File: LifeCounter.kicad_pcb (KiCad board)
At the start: 4 copper layers, 132.3 x 43.9 mm, 36 parts, among them IC1 STM32H562RGT6, IC2 AP3012KTR-E1, IC3 MCP73831T-2ATI_OT, IC4 AP2112K-3.3TRG1, J1 54104-4531, J2 USB_C_Receptacle_USB2.0_14P

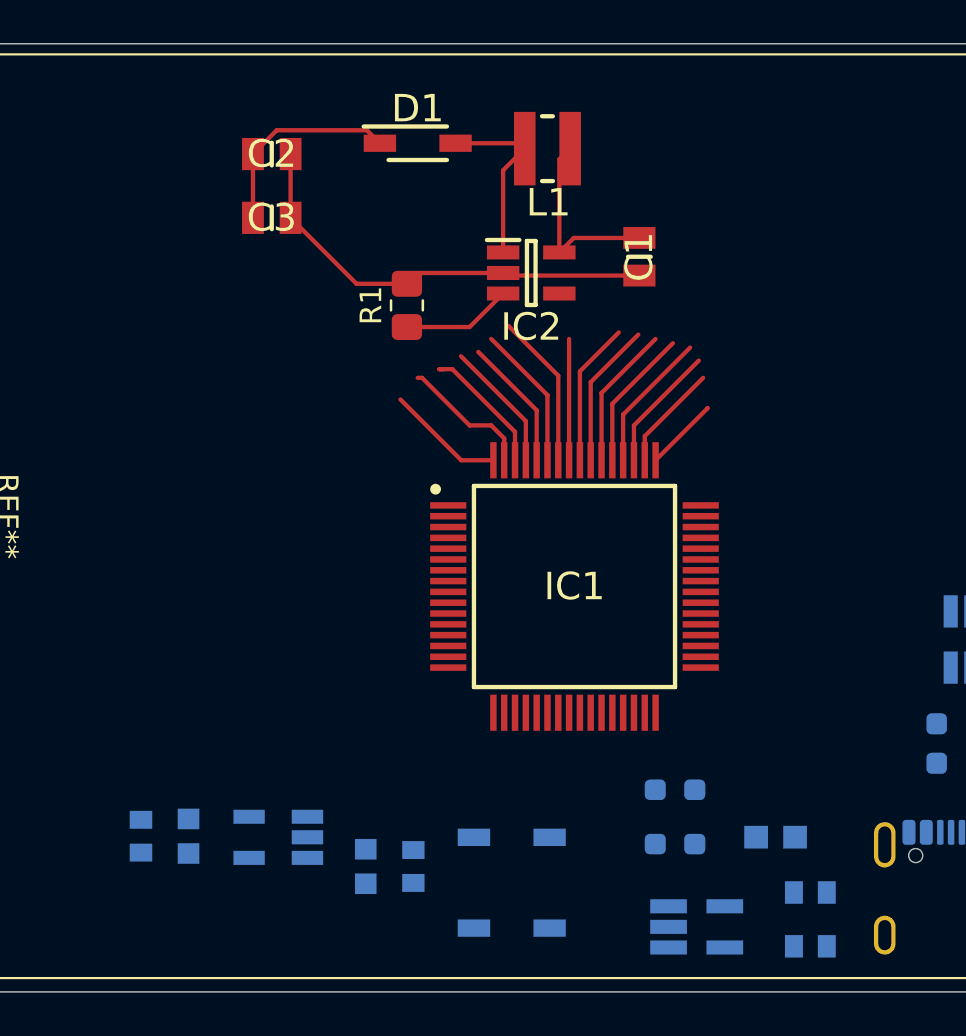
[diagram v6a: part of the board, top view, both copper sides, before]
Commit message: capacitor changes
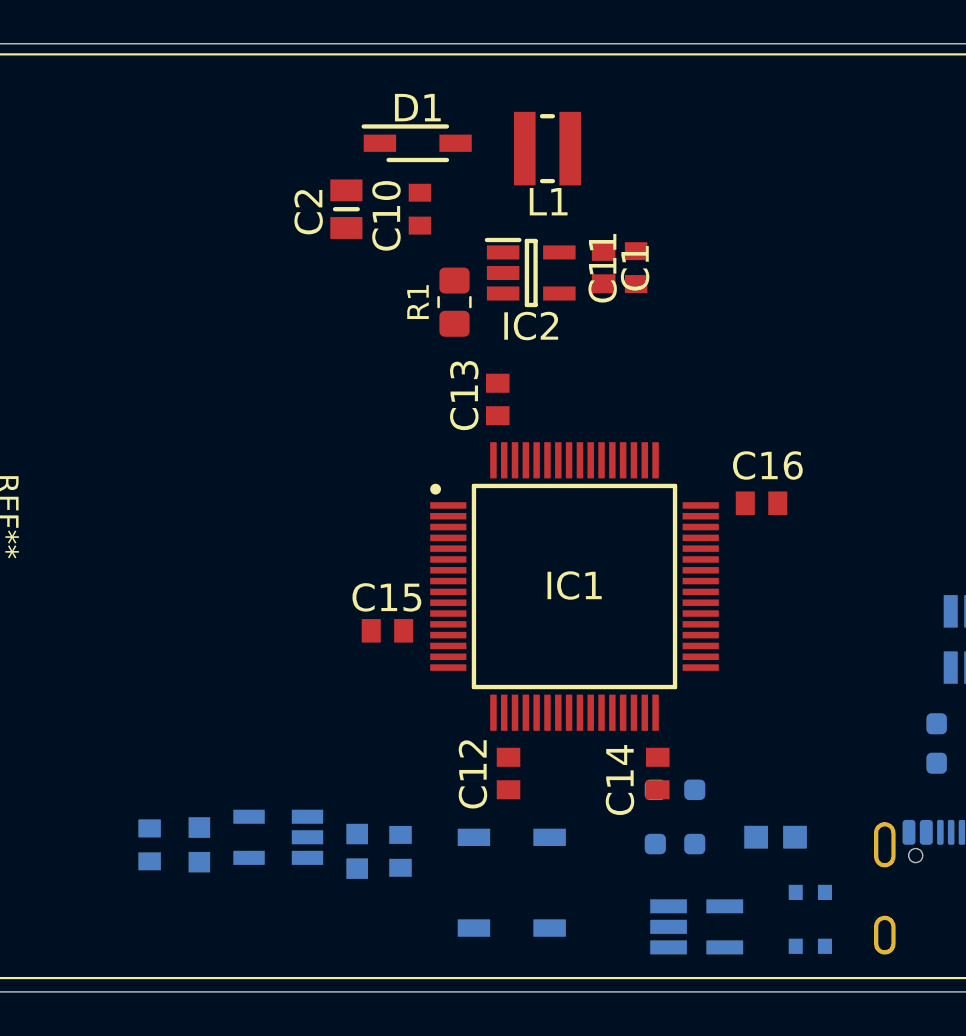
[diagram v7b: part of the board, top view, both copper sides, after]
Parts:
- added C11: 06033D104KAT2A, LifeCounter-Footprints:Kyocera_CAPC1608X90M, F.Cu at (173.6, 71.5)
- added C12: 06033D104KAT2A, LifeCounter-Footprints:Kyocera_CAPC1608X90M, F.Cu at (169.2, 94.9)
- added C13: 06033D104KAT2A, LifeCounter-Footprints:Kyocera_CAPC1608X90M, F.Cu at (168.7, 77.6)
- added C14: 06033D104KAT2A, LifeCounter-Footprints:Kyocera_CAPC1608X90M, F.Cu at (176.1, 94.9)
- added C15: 06033D104KAT2A, LifeCounter-Footprints:Kyocera_CAPC1608X90M, F.Cu at (163.6, 88.3)
- added C16: 06033D104KAT2A, LifeCounter-Footprints:Kyocera_CAPC1608X90M, F.Cu at (180.9, 82.4)
- C1: value CL21B105KBFNNNE -> CL10B105KO8NNNC; footprint LifeCounter-Footprints:Samsung_CAPC2012X135M -> LifeCounter-Footprints:Samsung_CAPC1608X90M
- C10: value C0603C104K8RACTU -> CL10B104KB8NNNC; footprint LifeCounter-Footprints:Kemet_C0603 -> LifeCounter-Footprints:Samsung_CAPC1608X90M; moved to F.Cu
- C3: value CL21B105KBFNNNE -> CL10B105KO8NNNC; footprint LifeCounter-Footprints:Samsung_CAPC2012X135M -> LifeCounter-Footprints:Samsung_CAPC1608X90M; moved to B.Cu
- C5, C6: value CL10A475KP8NNNC -> GRM188R61E106KA73D; footprint LifeCounter-Footprints:Samsung_CAPC1608X90M -> LifeCounter-Footprints:Murata_GRM18x
- C7: value CL10A106KP8NNNC -> CL10B105KO8NNNC
- C9: value CL10A106KP8NNNC -> C0603C104K8RACTU; footprint LifeCounter-Footprints:Samsung_CAPC1608X90M -> LifeCounter-Footprints:Kemet_C0603
- moved C10 30.9 mm to (165.1, 68.8)
- moved C3 29.5 mm to (152.6, 98.2), turned to -90 degrees
- moved C2 4.29 mm to (161.7, 68.8), turned to -90 degrees
- moved C9 2.73 mm to (154.9, 98.2)
- moved R1 2.21 mm to (166.7, 73.1)
- moved C7 0.92 mm to (164.2, 98.5)
- moved C8 0.81 mm to (162.2, 98.5)
- moved C1 0.52 mm to (175.1, 71.5)
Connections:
- C1 pad 2: Net-(IC2-GND) -> GND
- C10 pad 1: +3V3 -> Net-(D1-K)
- C2 pad 2: Net-(IC2-GND) -> GND
- C3 pad 1: Net-(D1-K) -> +3V3
- C3 pad 2: Net-(IC2-GND) -> GND
- C5 pad 1: /VBUS -> Net-(BT1-+)
- C6 pad 1: Net-(BT1-+) -> /VBUS
- IC2 pad 2: Net-(IC2-GND) -> GND
- R1 pad 2: Net-(IC2-GND) -> GND
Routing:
- net Net-(IC2-GND): track 20.6 -> 0.00 mm
- net Net-(D1-K): track 9.52 -> 0.00 mm
- net Net-(IC2-VIN): track 8.98 -> 0.00 mm
- net Net-(D1-A): track 8.52 -> 0.00 mm
- net unconnected-(IC1-PB6-Pad58): track 7.16 -> 0.00 mm
- net unconnected-(IC1-PB3-Pad55): track 6.72 -> 0.00 mm
- net unconnected-(IC1-PB7-Pad59): track 6.69 -> 0.00 mm
- net unconnected-(IC1-PB4-Pad56): track 6.66 -> 0.00 mm
- net unconnected-(IC1-PD2-Pad54): track 6.65 -> 0.00 mm
- net unconnected-(IC1-PC12-Pad53): track 6.57 -> 0.00 mm
- net unconnected-(IC1-PC11-Pad52): track 6.50 -> 0.00 mm
- net GND: track 6.45 -> 0.00 mm
- net unconnected-(IC1-VCAP_2-Pad62): track 6.21 -> 0.00 mm
- net unconnected-(IC1-BOOT0-Pad60): track 6.13 -> 0.00 mm
- net unconnected-(IC1-PB8-Pad61): track 6.05 -> 0.00 mm
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
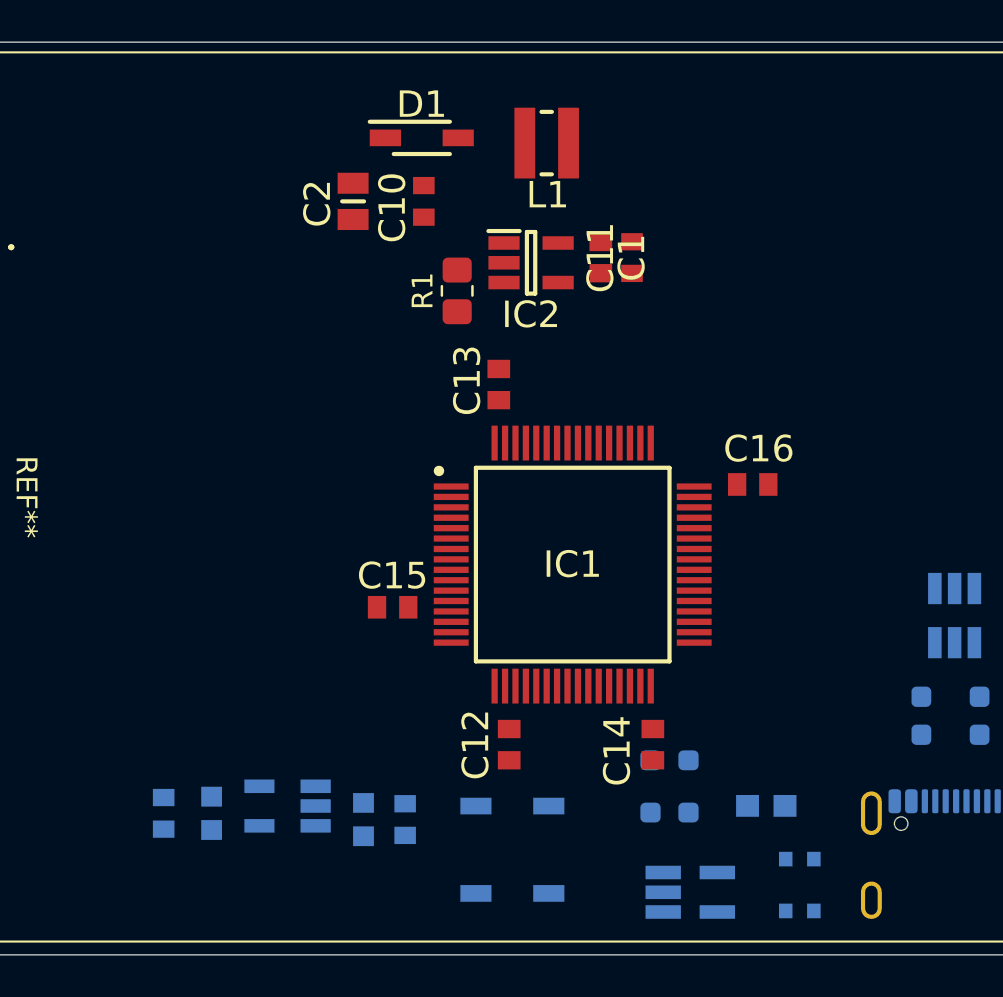
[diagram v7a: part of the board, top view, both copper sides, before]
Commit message: labeled the LCD pins and switched over to a 100 pin stm32 package
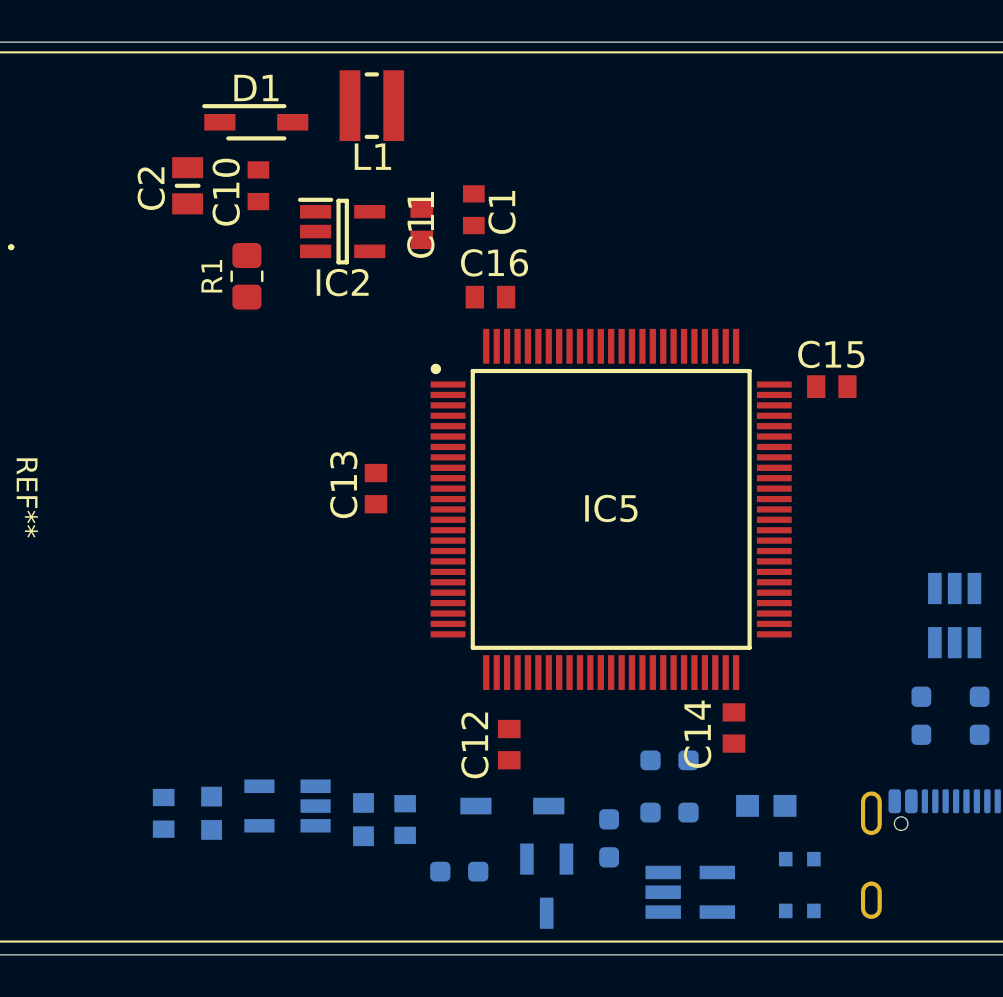
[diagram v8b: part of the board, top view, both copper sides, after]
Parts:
- removed D3: 1N5819HWQ-7-F, LifeCounter-Footprints:Diodes-Inc_SOD3716X145M
- removed IC1: STM32H562RGT6, LifeCounter-Footprints:LQFP-64_10x10mm_P0.5mm_STM32
- added IC5: STM32H562VGT6, LifeCounter-Footprints:STMicroelectronics_QFP50P1600X1600X160-100M, F.Cu at (174.1, 83.6)
- added Q1: AO3401A, LifeCounter-Footprints:Alpha&Omega_SOT95P280X125-3M, B.Cu at (171.0, 101.7)
- added R6: 100k, Resistor_SMD:R_0603_1608Metric_Pad0.98x0.95mm_HandSolder, B.Cu at (166.8, 101.0)
- added R7: 1k, Resistor_SMD:R_0603_1608Metric_Pad0.98x0.95mm_HandSolder, B.Cu at (174.0, 99.4)
- C1, C3, C7: value CL10B105KO8NNNC -> 1uF
- C10: value CL10B104KB8NNNC -> 100nF
- C11, C12, C13, C14, C15, C16: value 06033D104KAT2A -> 100nF
- C2: value CL21B105KBFNNNE -> 1uF
- C4: value CL10A106KP8NNNC -> 10uF
- C5, C6: value GRM188R61E106KA73D -> 10uF
- C8, C9: value C0603C104K8RACTU -> 100nF
- L1: value VLS3012CX-100M-1 -> 10uH
- R1: value 0805S8F820JT5E -> 62
- R4: value 2k -> 2k7
- moved C15 23.6 mm to (184.7, 77.7)
- moved C16 15.5 mm to (168.3, 73.4)
- moved R1 10.1 mm to (156.6, 72.4)
- moved IC2 9.17 mm to (161.2, 70.2)
- moved C11 8.75 mm to (165.0, 69.9)
- moved L1 8.59 mm to (162.6, 64.2)
- moved C10 7.99 mm to (157.2, 68.0)
- moved C2 7.99 mm to (153.8, 68.0)
- moved D1 7.99 mm to (157.1, 65.0)
- moved C1 7.94 mm to (167.5, 69.2)
- moved C13 7.73 mm to (162.8, 82.6)
- moved C14 3.98 mm to (180.0, 94.1)
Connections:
- net /VBUS renamed /Power_Management/VBUS
- net Net-(BT1-+) renamed /Power_Management/BAT+
- C10 pad 1: Net-(D1-K) -> /LCD_ANODE
- C12 pad 1: GND -> +3V3
- C12 pad 2: +3V3 -> GND
- C2 pad 1: Net-(D1-K) -> /LCD_ANODE
- D1 pad 1: Net-(D1-K) -> /LCD_ANODE
- IC2 pad 3: Net-(IC2-FB) -> /LCD_CATHODE
- IC2 pad 4: unconnected-(IC2-~{SHDN}-Pad4) -> /LCD_BL_EN
- J1 pad 10: unconnected-(J1-Pad10) -> GND
- J1 pad 11: unconnected-(J1-Pad11) -> GND
- J1 pad 12: unconnected-(J1-Pad12) -> GND
- J1 pad 13: unconnected-(J1-Pad13) -> GND
- J1 pad 14: unconnected-(J1-Pad14) -> GND
- J1 pad 15: unconnected-(J1-Pad15) -> GND
- J1 pad 16: unconnected-(J1-Pad16) -> GND
- J1 pad 17: unconnected-(J1-Pad17) -> GND
- J1 pad 18: unconnected-(J1-Pad18) -> GND
- J1 pad 19: unconnected-(J1-Pad19) -> GND
- J1 pad 2: unconnected-(J1-Pad2) -> GND
- J1 pad 20: unconnected-(J1-Pad20) -> GND
- J1 pad 21: unconnected-(J1-Pad21) -> /LCD_DB7
- J1 pad 22: unconnected-(J1-Pad22) -> /LCD_DB6
- J1 pad 23: unconnected-(J1-Pad23) -> /LCD_DB5
- J1 pad 24: unconnected-(J1-Pad24) -> /LCD_DB4
- J1 pad 25: unconnected-(J1-Pad25) -> /LCD_DB3
- J1 pad 26: unconnected-(J1-Pad26) -> /LCD_DB2
- J1 pad 27: unconnected-(J1-Pad27) -> /LCD_DB1
- J1 pad 28: unconnected-(J1-Pad28) -> /LCD_DB0
- J1 pad 29: unconnected-(J1-Pad29) -> /LCD_SDO
- J1 pad 3: unconnected-(J1-Pad3) -> GND
- J1 pad 30: unconnected-(J1-Pad30) -> +3V3
- J1 pad 31: unconnected-(J1-Pad31) -> /LCD_RD
- J1 pad 32: unconnected-(J1-Pad32) -> /LCD_RS
- J1 pad 33: unconnected-(J1-Pad33) -> /LCD_WR
- J1 pad 34: unconnected-(J1-Pad34) -> /LCD_CS
- J1 pad 35: unconnected-(J1-Pad35) -> /LCD_FMARK
- J1 pad 36: unconnected-(J1-Pad36) -> +3V3
- J1 pad 37: unconnected-(J1-Pad37) -> +3V3
- J1 pad 38: unconnected-(J1-Pad38) -> GND
- J1 pad 39: unconnected-(J1-Pad39) -> GND
- J1 pad 4: unconnected-(J1-Pad4) -> GND
- J1 pad 40: unconnected-(J1-Pad40) -> /LCD_ANODE
- J1 pad 41: unconnected-(J1-Pad41) -> /LCD_CATHODE
- J1 pad 5: unconnected-(J1-Pad5) -> GND
- J1 pad 6: unconnected-(J1-Pad6) -> /LCD_RESET
- J1 pad 7: unconnected-(J1-Pad7) -> +3V3
- J1 pad 8: unconnected-(J1-Pad8) -> +3V3
- J1 pad 9: unconnected-(J1-Pad9) -> GND
- R1 pad 1: Net-(IC2-FB) -> /LCD_CATHODE
